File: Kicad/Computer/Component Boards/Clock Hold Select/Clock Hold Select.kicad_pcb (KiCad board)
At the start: 2 copper layers, 26.7 x 59.7 mm, 20 parts, among them IC1 AP7365-33WG-7, IC2 74LVC244APW,118, IC4 74LVC244APW,118, IC5 74LVC244APW,118, IC6 74LVC32APW,118, J1 Conn_02x20_Counter_Clockwise

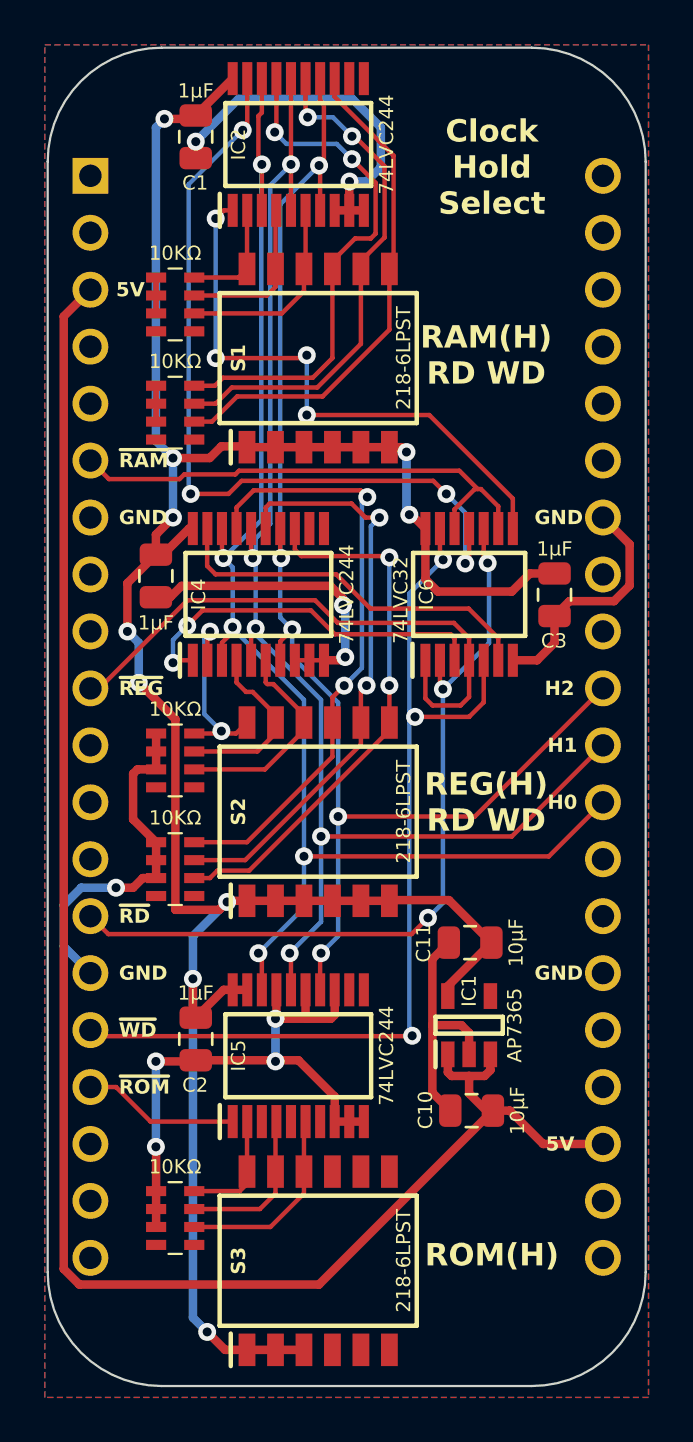
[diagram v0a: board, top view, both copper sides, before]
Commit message: Include ROM read and write clock holds.
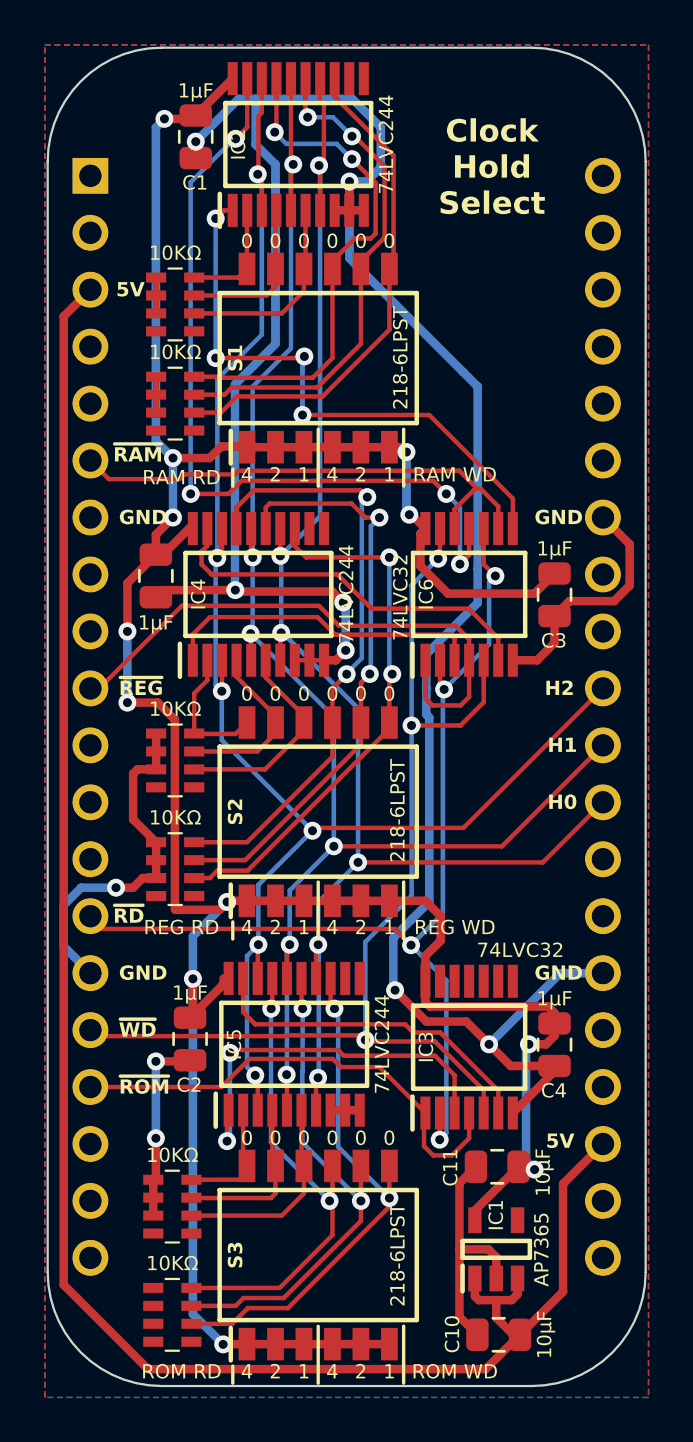
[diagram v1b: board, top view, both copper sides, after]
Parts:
- added C4: 1μF, SamacSys_Parts:C_0805, F.Cu at (109.6, 97.2)
- added IC3: 74LVC32APW,118, SamacSys_Parts:SOP65P640X110-14N, F.Cu at (105.8, 97.3)
- added RN6: CAY16-103J4LF, SamacSys_Parts:CAY16-J4, F.Cu at (92.6, 109.2)
- moved C11 10.1 mm to (107.1, 102.6)
- moved IC1 10.1 mm to (107.0, 106.3)
- moved C10 10.1 mm to (107.1, 110.1)
- moved IC5 0.54 mm to (98.0, 97.2)
- moved RN5 0.52 mm to (92.6, 104.4)
- moved RN2 0.40 mm to (92.7, 68.6)
- moved C2 0.25 mm to (93.3, 96.9)
- moved S3 0.25 mm to (99.1, 106.6)
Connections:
- net /ROM H0 renamed /ROM RD H2
- net /ROM H1 renamed /ROM RD H1
- net /ROM H2 renamed /ROM RD H0
- IC2 pad 13: /RAM WD H2 -> /RAM WD H0
- IC2 pad 14: /H2 -> /H0
- IC2 pad 17: /RAM WD H0 -> /RAM WD H2
- IC2 pad 18: /H0 -> /H2
- IC2 pad 2: /RAM RD H0 -> /RAM RD H2
- IC2 pad 3: /H0 -> /H2
- IC2 pad 6: /RAM RD H2 -> /RAM RD H0
- IC2 pad 7: /H2 -> /H0
- IC4 pad 13: /REG WD H2 -> /REG WD H0
- IC4 pad 14: /H2 -> /H0
- IC4 pad 17: /REG WD H0 -> /REG WD H2
- IC4 pad 18: /H0 -> /H2
- IC4 pad 2: /REG RD H0 -> /REG RD H2
- IC4 pad 3: /H0 -> /H2
- IC4 pad 6: /REG RD H2 -> /REG RD H0
- IC4 pad 7: /H2 -> /H0
- IC5 pad 1: /~{Device ROM} -> /~{ROM}+~{RD}
- IC5 pad 13: /GND -> /ROM WD H0
- IC5 pad 14: /H2 -> /H0
- IC5 pad 15: /GND -> /ROM WD H1
- IC5 pad 17: /GND -> /ROM WD H2
- IC5 pad 18: /H0 -> /H2
- IC5 pad 19: /3.3V -> /~{ROM}+~{WD}
- IC5 pad 3: unconnected-(IC5-2Y0-Pad3) -> /H2
- IC5 pad 5: unconnected-(IC5-2Y1-Pad5) -> /H1
- IC5 pad 7: unconnected-(IC5-2Y2-Pad7) -> /H0
- RN1 pad 6: /RAM RD H2 -> /RAM RD H0
- RN1 pad 8: /RAM RD H0 -> /RAM RD H2
- RN2 pad 6: /RAM WD H2 -> /RAM WD H0
- RN2 pad 8: /RAM WD H0 -> /RAM WD H2
- RN3 pad 6: /REG RD H2 -> /REG RD H0
- RN3 pad 8: /REG RD H0 -> /REG RD H2
- RN4 pad 6: /REG WD H2 -> /REG WD H0
- RN4 pad 8: /REG WD H0 -> /REG WD H2
- S1 pad 10: /RAM RD H2 -> /RAM RD H0
- S1 pad 12: /RAM RD H0 -> /RAM RD H2
- S1 pad 7: /RAM WD H2 -> /RAM WD H0
- S1 pad 9: /RAM WD H0 -> /RAM WD H2
- S2 pad 10: /REG RD H2 -> /REG RD H0
- S2 pad 12: /REG RD H0 -> /REG RD H2
- S2 pad 7: /REG WD H2 -> /REG WD H0
- S2 pad 9: /REG WD H0 -> /REG WD H2
- S3 pad 4: unconnected-(S3-Pad4) -> /3.3V
- S3 pad 5: unconnected-(S3-Pad5) -> /3.3V
- S3 pad 6: unconnected-(S3-Pad6) -> /3.3V
- S3 pad 7: unconnected-(S3-Pad7) -> /ROM WD H0
- S3 pad 8: unconnected-(S3-Pad8) -> /ROM WD H1
- S3 pad 9: unconnected-(S3-Pad9) -> /ROM WD H2
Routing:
- net /GND: track 97.7 -> 160.9 mm, vias 9 -> 10
- net /ROM WD H0: track 0.00 -> 23.7 mm, vias 0 -> 2
- net /ROM WD H1: track 0.00 -> 22.6 mm, vias 0 -> 2
- net /ROM WD H2: track 0.00 -> 21.5 mm, vias 0 -> 2
- net /3.3V: track 113.3 -> 134.0 mm, vias 10 -> 12
- net /~{ROM}+~{RD}: track 0.00 -> 17.5 mm, vias 0 -> 2
- net /~{ROM}+~{WD}: track 0.00 -> 15.3 mm
- net /~{Device ROM}: track 6.98 -> 21.5 mm
- net /~{RD}: track 35.6 -> 47.2 mm, vias 3 -> 4
- net /H2: track 62.0 -> 71.8 mm, vias 5 -> 6
- net /H1: track 62.3 -> 69.3 mm, vias 5 -> 6
- net /~{WD}: track 42.9 -> 49.0 mm
- net /5V: track 77.8 -> 82.9 mm
- net /H0: track 63.3 -> 67.2 mm, vias 5 -> 6
- net /RAM RD H2: track 8.84 -> 5.11 mm
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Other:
- board text added: "0"
- board text added: "1"
- board text added: "2"
- board text added: "4"
- board text added: "RAM RD"
- board text added: "RAM WD"
- board text added: "REG RD"
- board text added: "REG WD"
- board text added: "ROM RD"
- board text added: "ROM WD"
- board text removed: "RAM(H) RD WD"
- board text removed: "REG(H) RD WD"
- board text removed: "ROM(H)"

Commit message: Splitting Via Schematics into separate projects.
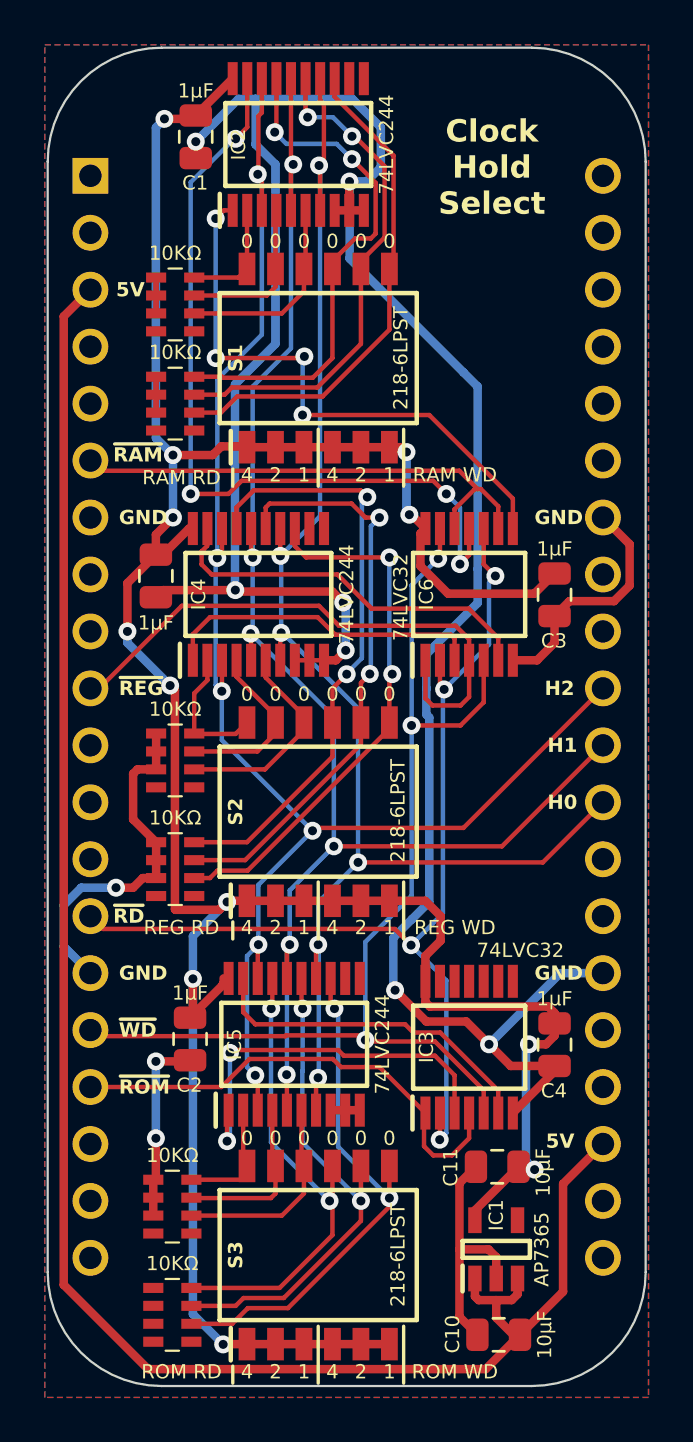
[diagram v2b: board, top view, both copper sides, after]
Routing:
- net /~{Device RAM}: track 22.6 -> 21.6 mm
- net /3.3V: track 134.0 -> 133.2 mm
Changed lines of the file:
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@@
   (segment (start 103.841 93.211458) (end 104.521 92.531458) (width 0.38) (layer "F.Cu") (net 3))
   (segment (start 98.425 90.754) (end 99.695 90.754) (width 0.38) (layer "F.Cu") (net 3))
+  (segment (start 94.742 70.485) (end 94.354 70.873) (width 0.38) (layer "F.Cu") (net 3))
   (segment (start 94.831006 110.528) (end 94.8206 110.538406) (width 0.38) (layer "F.Cu") (net 3))
   (segment (start 97.155 110.528) (end 98.425 110.528) (width 0.38) (layer "F.Cu") (net 3))
@@
   (segment (start 90.551 78.74) (end 90.551 76.586) (width 0.38) (layer "F.Cu") (net 3))
   (segment (start 93.468 74.151) (end 93.301 74.151) (width 0.38) (layer "F.Cu") (net 3))
-  (segment (start 94.21994 71.00706) (end 92.583 71.00706) (width 0.38) (layer "F.Cu") (net 3))
   (segment (start 95.047 90.754) (end 94.996 90.805) (width 0.38) (layer "F.Cu") (net 3))
   (segment (start 109.219996 97.155004) (end 108.457998 97.155004) (width 0.38) (layer "F.Cu") (net 3))
   (segment (start 98.425 110.528) (end 99.695 110.528) (width 0.38) (layer "F.Cu") (net 3))
   (segment (start 99.695 110.528) (end 100.965 110.528) (width 0.38) (layer "F.Cu") (net 3))
-  (segment (start 92.671 82.678) (end 91.908 81.915) (width 0.38) (layer "F.Cu") (net 3))
   (segment (start 109.601 96.221) (end 109.601 95.758) (width 0.38) (layer "F.Cu") (net 3))
-  (segment (start 92.671 91.135558) (end 92.671 82.678) (width 0.38) (layer "F.Cu") (net 3))
-  (segment (start 94.742 70.485) (end 94.21994 71.00706) (width 0.38) (layer "F.Cu") (net 3))
   (segment (start 98.425 70.523) (end 99.695 70.523) (width 0.38) (layer "F.Cu") (net 3))
   (segment (start 90.551 76.586) (end 91.821001 75.315999) (width 0.38) (layer "F.Cu") (net 3))
@@
   (segment (start 109.601 96.774) (end 109.219996 97.155004) (width 0.38) (layer "F.Cu") (net 3))
   (segment (start 97.155 70.523) (end 98.425 70.523) (width 0.38) (layer "F.Cu") (net 3))
+  (segment (start 92.671 91.135558) (end 92.671 81.368) (width 0.38) (layer "F.Cu") (net 3))
   (segment (start 109.601 95.758) (end 109.3145 95.4715) (width 0.38) (layer "F.Cu") (net 3))
   (segment (start 94.841 94.471) (end 93.345 95.967) (width 0.38) (layer "F.Cu") (net 3))
@@
   (segment (start 103.841 95.273756) (end 103.841 94.344) (width 0.38) (layer "F.Cu") (net 3))
   (segment (start 104.521 92.531458) (end 104.521 91.440001) (width 0.38) (layer "F.Cu") (net 3))
-  (segment (start 92.691 91.155558) (end 92.671 91.135558) (width 0.38) (layer "F.Cu") (net 3))
   (segment (start 95.243558 54.085) (end 93.599 55.729558) (width 0.38) (layer "F.Cu") (net 3))
-  (segment (start 91.908 81.915) (end 90.551 81.915) (width 0.38) (layer "F.Cu") (net 3))
   (segment (start 95.885 90.754) (end 97.155 90.754) (width 0.38) (layer "F.Cu") (net 3))
+  (segment (start 92.671 81.368) (end 92.456 81.153) (width 0.38) (layer "F.Cu") (net 3))
   (segment (start 108.700241 77.055759) (end 109.601 76.155) (width 0.38) (layer "F.Cu") (net 3))
+  (segment (start 94.996 90.805) (end 94.645442 91.155558) (width 0.38) (layer "F.Cu") (net 3))
   (segment (start 93.301 74.151) (end 92.136001 75.315999) (width 0.38) (layer "F.Cu") (net 3))
   (segment (start 93.472 94.234) (end 93.472 95.585998) (width 0.38) (layer "F.Cu") (net 3))
-  (segment (start 94.645442 91.155558) (end 92.691 91.155558) (width 0.38) (layer "F.Cu") (net 3))
   (segment (start 100.965 110.528) (end 102.235 110.528) (width 0.38) (layer "F.Cu") (net 3))
   (segment (start 100.965 90.754) (end 102.235 90.754) (width 0.38) (layer "F.Cu") (net 3))
+  (segment (start 94.645442 91.155558) (end 92.691 91.155558) (width 0.38) (layer "F.Cu") (net 3))
   (segment (start 103.841 74.151) (end 103.223 73.533) (width 0.38) (layer "F.Cu") (net 3))
   (segment (start 95.885 90.754) (end 95.047 90.754) (width 0.38) (layer "F.Cu") (net 3))
-  (segment (start 95.847 70.485) (end 94.742 70.485) (width 0.38) (layer "F.Cu") (net 3))
-  (segment (start 94.996 90.805) (end 94.645442 91.155558) (width 0.38) (layer "F.Cu") (net 3))
+  (segment (start 94.354 70.873) (end 92.583 70.873) (width 0.38) (layer "F.Cu") (net 3))
   (segment (start 103.223 73.533) (end 103.124 73.533) (width 0.38) (layer "F.Cu") (net 3))
   (segment (start 95.885 70.523) (end 97.155 70.523) (width 0.38) (layer "F.Cu") (net 3))
   (segment (start 104.854532 77.055759) (end 108.700241 77.055759) (width 0.38) (layer "F.Cu") (net 3))
   (segment (start 95.885 110.528) (end 97.155 110.528) (width 0.38) (layer "F.Cu") (net 3))
+  (segment (start 95.847 70.485) (end 94.742 70.485) (width 0.38) (layer "F.Cu") (net 3))
   (segment (start 107.995 102.616) (end 108.585 102.616) (width 0.38) (layer "F.Cu") (net 3))
   (segment (start 99.695 70.523) (end 100.965 70.523) (width 0.38) (layer "F.Cu") (net 3))
   (segment (start 99.695 90.754) (end 100.965 90.754) (width 0.38) (layer "F.Cu") (net 3))
+  (segment (start 92.691 91.155558) (end 92.671 91.135558) (width 0.38) (layer "F.Cu") (net 3))
   (segment (start 106.05 104.561) (end 107.995 102.616) (width 0.38) (layer "F.Cu") (net 3))
   (via (at 93.472 94.234) (size 0.8) (drill 0.4) (layers "F.Cu" "B.Cu") (net 3))
-  (via (at 90.551 81.915) (size 0.8) (drill 0.4) (layers "F.Cu" "B.Cu") (net 3))
+  (via (at 92.456 81.153) (size 0.8) (drill 0.4) (layers "F.Cu" "B.Cu") (net 3))
   (via (at 90.551 78.74) (size 0.8) (drill 0.4) (layers "F.Cu" "B.Cu") (net 3))
   (via (at 108.711995 102.742995) (size 0.8) (drill 0.4) (layers "F.Cu" "B.Cu") (net 3))
@@
   (via (at 92.583 73.66) (size 0.8) (drill 0.4) (layers "F.Cu" "B.Cu") (net 3))
   (via (at 94.996 90.805) (size 0.8) (drill 0.4) (layers "F.Cu" "B.Cu") (net 3))
-  (via (at 92.583 71.00706) (size 0.8) (drill 0.4) (layers "F.Cu" "B.Cu") (net 3))
+  (via (at 92.583 70.873) (size 0.8) (drill 0.4) (layers "F.Cu" "B.Cu") (net 3))
   (via (at 102.997 70.739) (size 0.8) (drill 0.4) (layers "F.Cu" "B.Cu") (net 3))
   (via (at 108.457998 97.155004) (size 0.8) (drill 0.4) (layers "F.Cu" "B.Cu") (net 3))
   (segment (start 108.331 102.362) (end 108.331 97.282002) (width 0.38) (layer "B.Cu") (net 3))
-  (segment (start 91.821 56.261) (end 91.821 70.24506) (width 0.38) (layer "B.Cu") (net 3))
   (segment (start 93.472 109.189806) (end 94.8206 110.538406) (width 0.38) (layer "B.Cu") (net 3))
+  (segment (start 90.551 79.248) (end 92.456 81.153) (width 0.38) (layer "B.Cu") (net 3))
   (segment (start 94.996 90.805) (end 93.472 92.329) (width 0.38) (layer "B.Cu") (net 3))
+  (segment (start 91.821 56.261) (end 91.821 70.111) (width 0.38) (layer "B.Cu") (net 3))
   (segment (start 93.472 94.234) (end 93.472 109.189806) (width 0.38) (layer "B.Cu") (net 3))
   (segment (start 102.997 73.406) (end 103.124 73.533) (width 0.38) (layer "B.Cu") (net 3))
+  (segment (start 108.711995 102.742995) (end 108.331 102.362) (width 0.38) (layer "B.Cu") (net 3))
+  (segment (start 90.551 78.74) (end 90.551 79.248) (width 0.38) (layer "B.Cu") (net 3))
+  (segment (start 91.821 70.111) (end 92.583 70.873) (width 0.38) (layer "B.Cu") (net 3))
+  (segment (start 93.472 92.329) (end 93.472 94.234) (width 0.38) (layer "B.Cu") (net 3))
+  (segment (start 92.583 73.66) (end 92.583 70.873) (width 0.38) (layer "B.Cu") (net 3))
+  (segment (start 102.997 70.739) (end 102.997 73.406) (width 0.38) (layer "B.Cu") (net 3))
+  (segment (start 108.331 97.282002) (end 108.457998 97.155004) (width 0.38) (layer "B.Cu") (net 3))
   (segment (start 92.202 55.88) (end 91.821 56.261) (width 0.38) (layer "B.Cu") (net 3))
-  (segment (start 108.711995 102.742995) (end 108.331 102.362) (width 0.38) (layer "B.Cu") (net 3))
-  (segment (start 93.472 92.329) (end 93.472 94.234) (width 0.38) (layer "B.Cu") (net 3))
-  (segment (start 92.583 71.00706) (end 92.583 73.66) (width 0.38) (layer "B.Cu") (net 3))
-  (segment (start 102.997 70.739) (end 102.997 73.406) (width 0.38) (layer "B.Cu") (net 3))
-  (segment (start 90.551 78.74) (end 90.551 81.915) (width 0.38) (layer "B.Cu") (net 3))
-  (segment (start 108.331 97.282002) (end 108.457998 97.155004) (width 0.38) (layer "B.Cu") (net 3))
-  (segment (start 91.821 70.24506) (end 92.583 71.00706) (width 0.38) (layer "B.Cu") (net 3))
   (segment (start 107.741 72.816) (end 104.013 69.088) (width 0.2) (layer "F.Cu") (net 37))
   (segment (start 94.852 59.961) (end 94.488 60.325) (width 0.2) (layer "F.Cu") (net 37))
@@
   (segment (start 107.091 79.0395) (end 105.7755 77.724) (width 0.2) (layer "F.Cu") (net 46))
   (segment (start 93.859 75.171828) (end 94.107 74.923828) (width 0.2) (layer "F.Cu") (net 46))
-  (segment (start 93.08295 71.737) (end 95.363965 71.737) (width 0.2) (layer "F.Cu") (net 47))
+  (segment (start 89.353 71.573) (end 105.355 71.573) (width 0.2) (layer "F.Cu") (net 47))
   (segment (start 105.141 73.294) (end 106.045 72.39) (width 0.2) (layer "F.Cu") (net 47))
-  (segment (start 95.363965 71.737) (end 95.527964 71.573) (width 0.2) (layer "F.Cu") (net 47))
   (segment (start 107.091 73.1635) (end 107.091 74.151) (width 0.2) (layer "F.Cu") (net 47))
-  (segment (start 89.727 71.947) (end 92.87295 71.947) (width 0.2) (layer "F.Cu") (net 47))
-  (segment (start 92.87295 71.947) (end 93.08295 71.737) (width 0.2) (layer "F.Cu") (net 47))
-  (segment (start 95.527964 71.573) (end 105.355 71.573) (width 0.2) (layer "F.Cu") (net 47))
   (segment (start 106.045 72.39) (end 106.3175 72.39) (width 0.2) (layer "F.Cu") (net 47))
-  (segment (start 88.9 71.12) (end 89.727 71.947) (width 0.2) (layer "F.Cu") (net 47))
+  (segment (start 105.355 71.573) (end 106.172 72.39) (width 0.2) (layer "F.Cu") (net 47))
   (segment (start 106.3175 72.39) (end 107.091 73.1635) (width 0.2) (layer "F.Cu") (net 47))
   (segment (start 105.141 74.151) (end 105.141 73.294) (width 0.2) (layer "F.Cu") (net 47))
-  (segment (start 105.355 71.573) (end 106.172 72.39) (width 0.2) (layer "F.Cu") (net 47))
   (segment (start 94.742 99.06) (end 95.993 97.809) (width 0.2) (layer "F.Cu") (net 50))
   (segment (start 104.188896 102.108) (end 103.778846 101.69795) (width 0.2) (layer "F.Cu") (net 50))

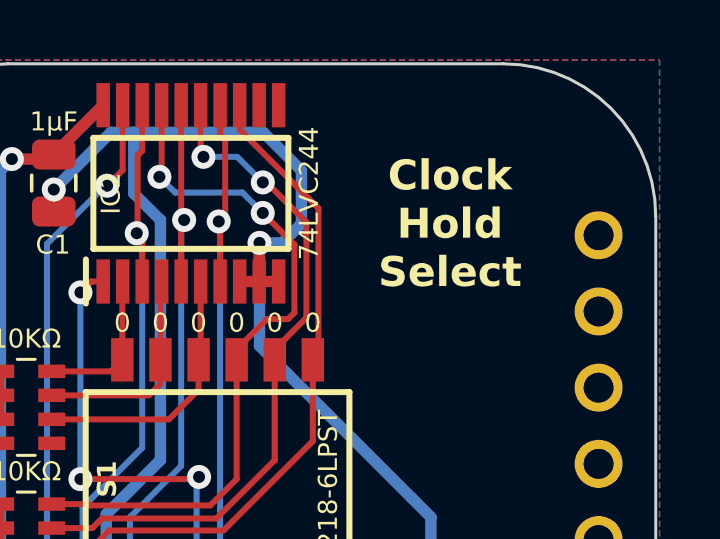
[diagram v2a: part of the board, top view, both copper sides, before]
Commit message: Added version number to component boards.
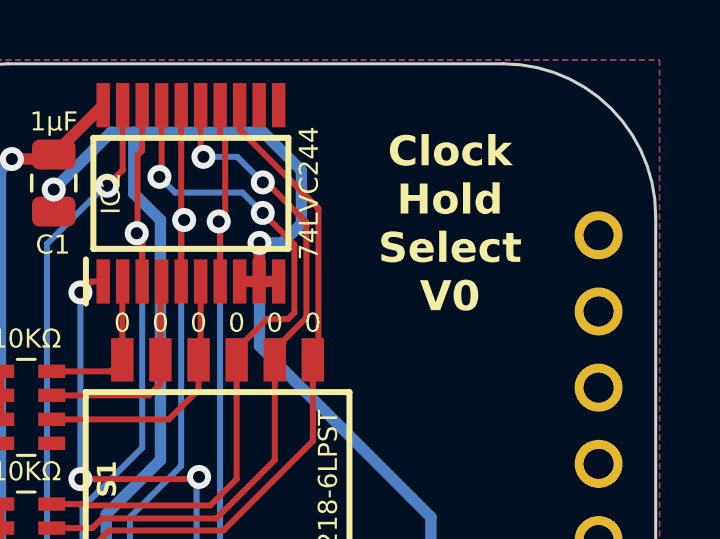
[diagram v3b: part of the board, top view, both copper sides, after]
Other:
- board text added: "Clock Hold Select V0"
- board text removed: "Clock Hold Select"
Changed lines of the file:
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@@
     (effects (font (size 0.635 0.635) (thickness 0.15)))
   )
-  (gr_text "Clock\nHold\nSelect" (at 106.807 58.039) (layer "F.SilkS" knockout)
+  (gr_text "Clock\nHold\nSelect\nV0" (at 106.807 58.039) (layer "F.SilkS" knockout)
     (effects (font (size 1 1) (thickness 0.2) bold))
   )
